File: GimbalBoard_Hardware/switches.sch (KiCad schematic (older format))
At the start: 31 parts

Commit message: connected everything up and changed power to accomodate teensy instead of tiva
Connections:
- net +3V3 renamed 3.3VL
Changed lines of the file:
@@
 $Descr A4 11693 8268
 encoding utf-8
-Sheet 4 7
+Sheet 4 8
 Title ""
 Date ""
@@
 $EndDescr
 $Comp
-L power:+3.3V #PWR?
-U 1 1 615E22D3
-P 1550 1200
-F 0 "#PWR?" H 1550 1050 50  0001 C CNN
-F 1 "+3.3V" H 1565 1373 50  0000 C CNN
-F 2 "" H 1550 1200 50  0001 C CNN
-F 3 "" H 1550 1200 50  0001 C CNN
-	1    1550 1200
-	1    0    0    -1
-$EndComp
-$Comp
 L Switch:SW_Push SW?
 U 1 1 615E41DD
@@
 Wire Wire Line
 	1550 5500 1550 4850
-$Comp
-L power:GND #PWR?
-U 1 1 615F842D
-P 3650 6300
-F 0 "#PWR?" H 3650 6050 50  0001 C CNN
-F 1 "GND" H 3655 6127 50  0000 C CNN
-F 2 "" H 3650 6300 50  0001 C CNN
-F 3 "" H 3650 6300 50  0001 C CNN
-	1    3650 6300
-	1    0    0    -1
-$EndComp
 Wire Wire Line
 	3350 1550 3650 1550
@@
 Wire Wire Line
 	3650 6150 3650 6300
-$Comp
-L power:+3.3V #PWR?
-U 1 1 61616E07
-P 4650 1450
-F 0 "#PWR?" H 4650 1300 50  0001 C CNN
-F 1 "+3.3V" H 4665 1623 50  0000 C CNN
-F 2 "" H 4650 1450 50  0001 C CNN
-F 3 "" H 4650 1450 50  0001 C CNN
-	1    4650 1450
-	1    0    0    -1
-$EndComp
 $Comp
 L Device:LED D?
@@
 Wire Wire Line
 	7400 2550 6650 2550
-$Comp
-L power:GND #PWR?
-U 1 1 61657CDC
-P 7400 3100
-F 0 "#PWR?" H 7400 2850 50  0001 C CNN
-F 1 "GND" H 7405 2927 50  0000 C CNN
-F 2 "" H 7400 3100 50  0001 C CNN
-F 3 "" H 7400 3100 50  0001 C CNN
-	1    7400 3100
-	1    0    0    -1
-$EndComp
 Wire Wire Line
 	5650 1900 5650 2150
@@
 Wire Wire Line
 	7400 1900 7400 2550
+Text HLabel 1550 1200 1    50   Input ~ 0
+3.3VL
+Text HLabel 3650 6300 3    50   Input ~ 0
+GND
+Text HLabel 4650 1450 1    50   Input ~ 0
+3.3VL
+Text HLabel 7400 3100 3    50   Input ~ 0
+GND
 $EndSCHEMATC

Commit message: added more text
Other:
- note added: "Digital/Manual Switch"
- note added: "Manual Servo Switches"
- moved on the sheet: D?, R?, SW?

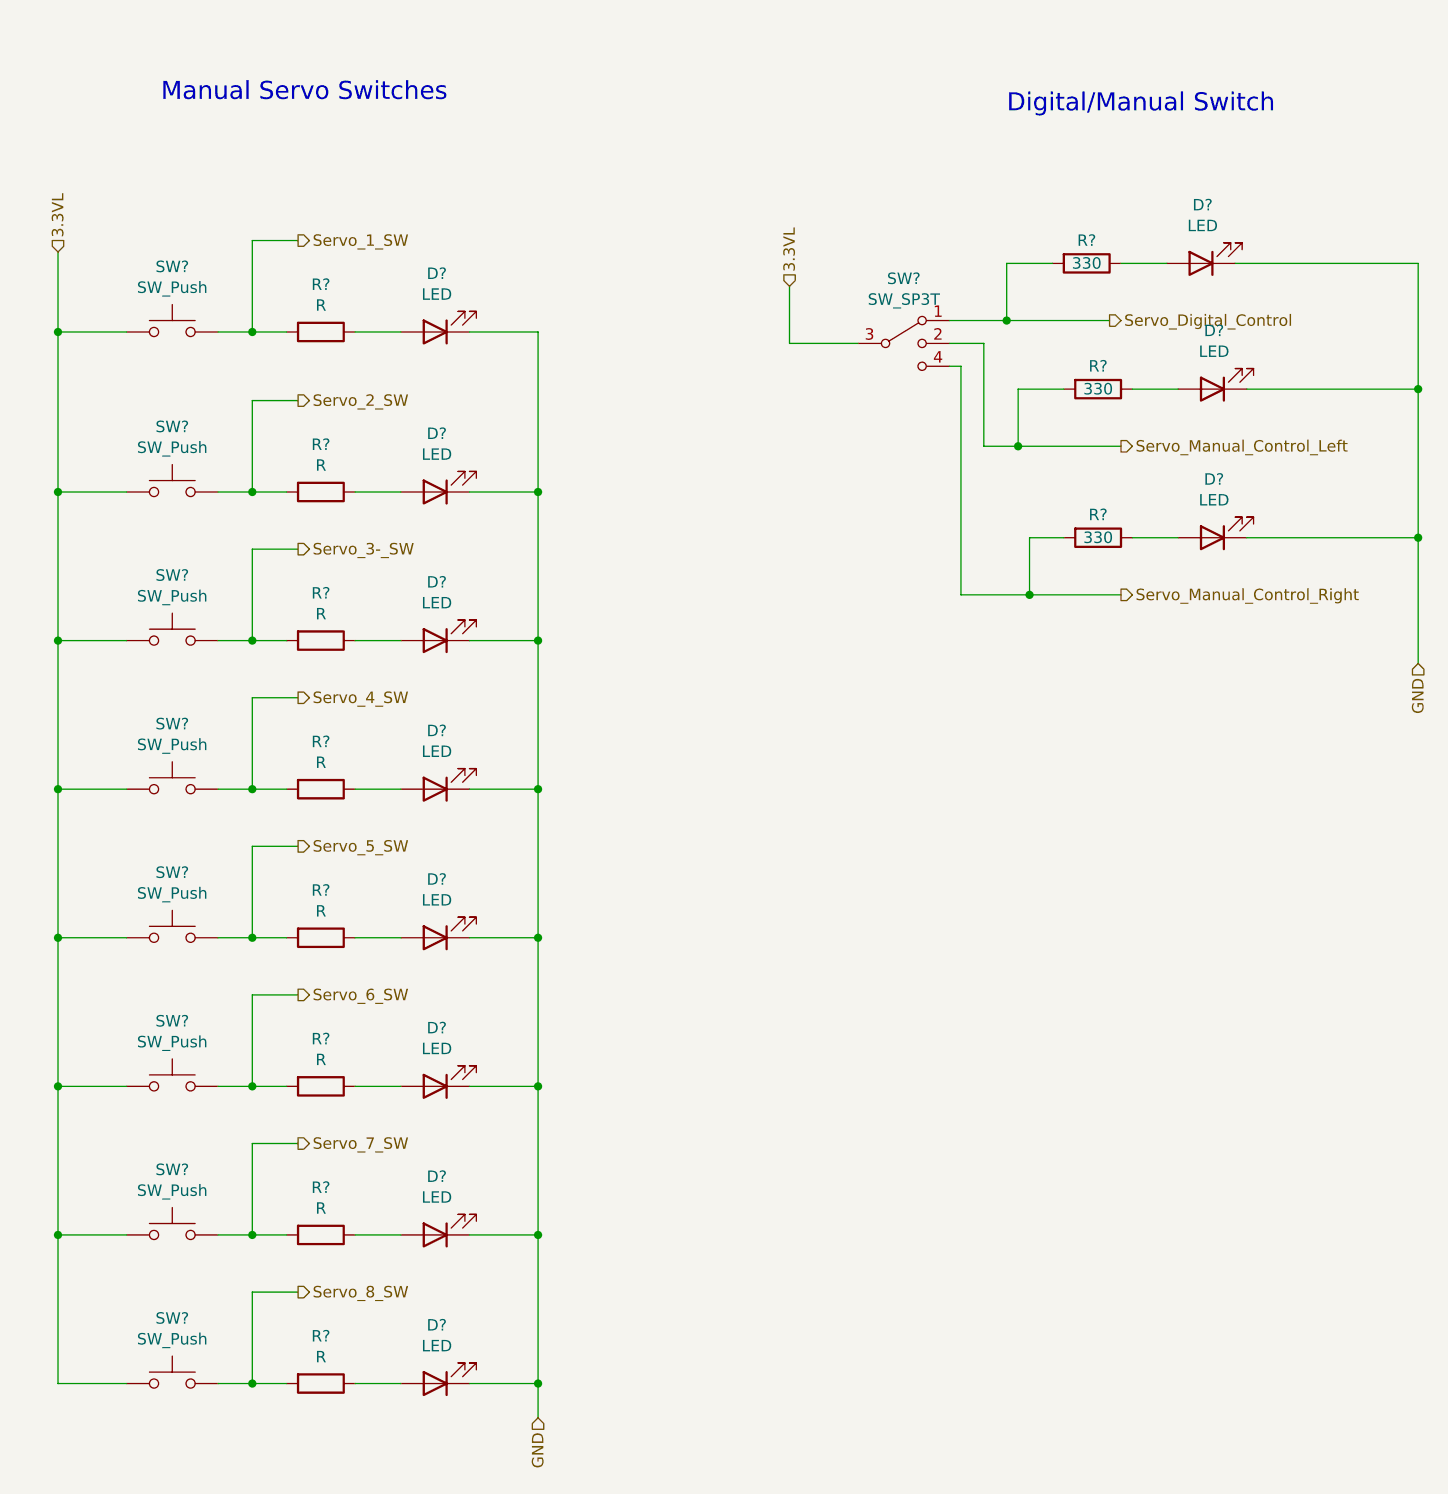
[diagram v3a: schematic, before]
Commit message: added labels, numbered everything, added no connection to pins. Still can't get past a couple pf errors in the electrical rules check
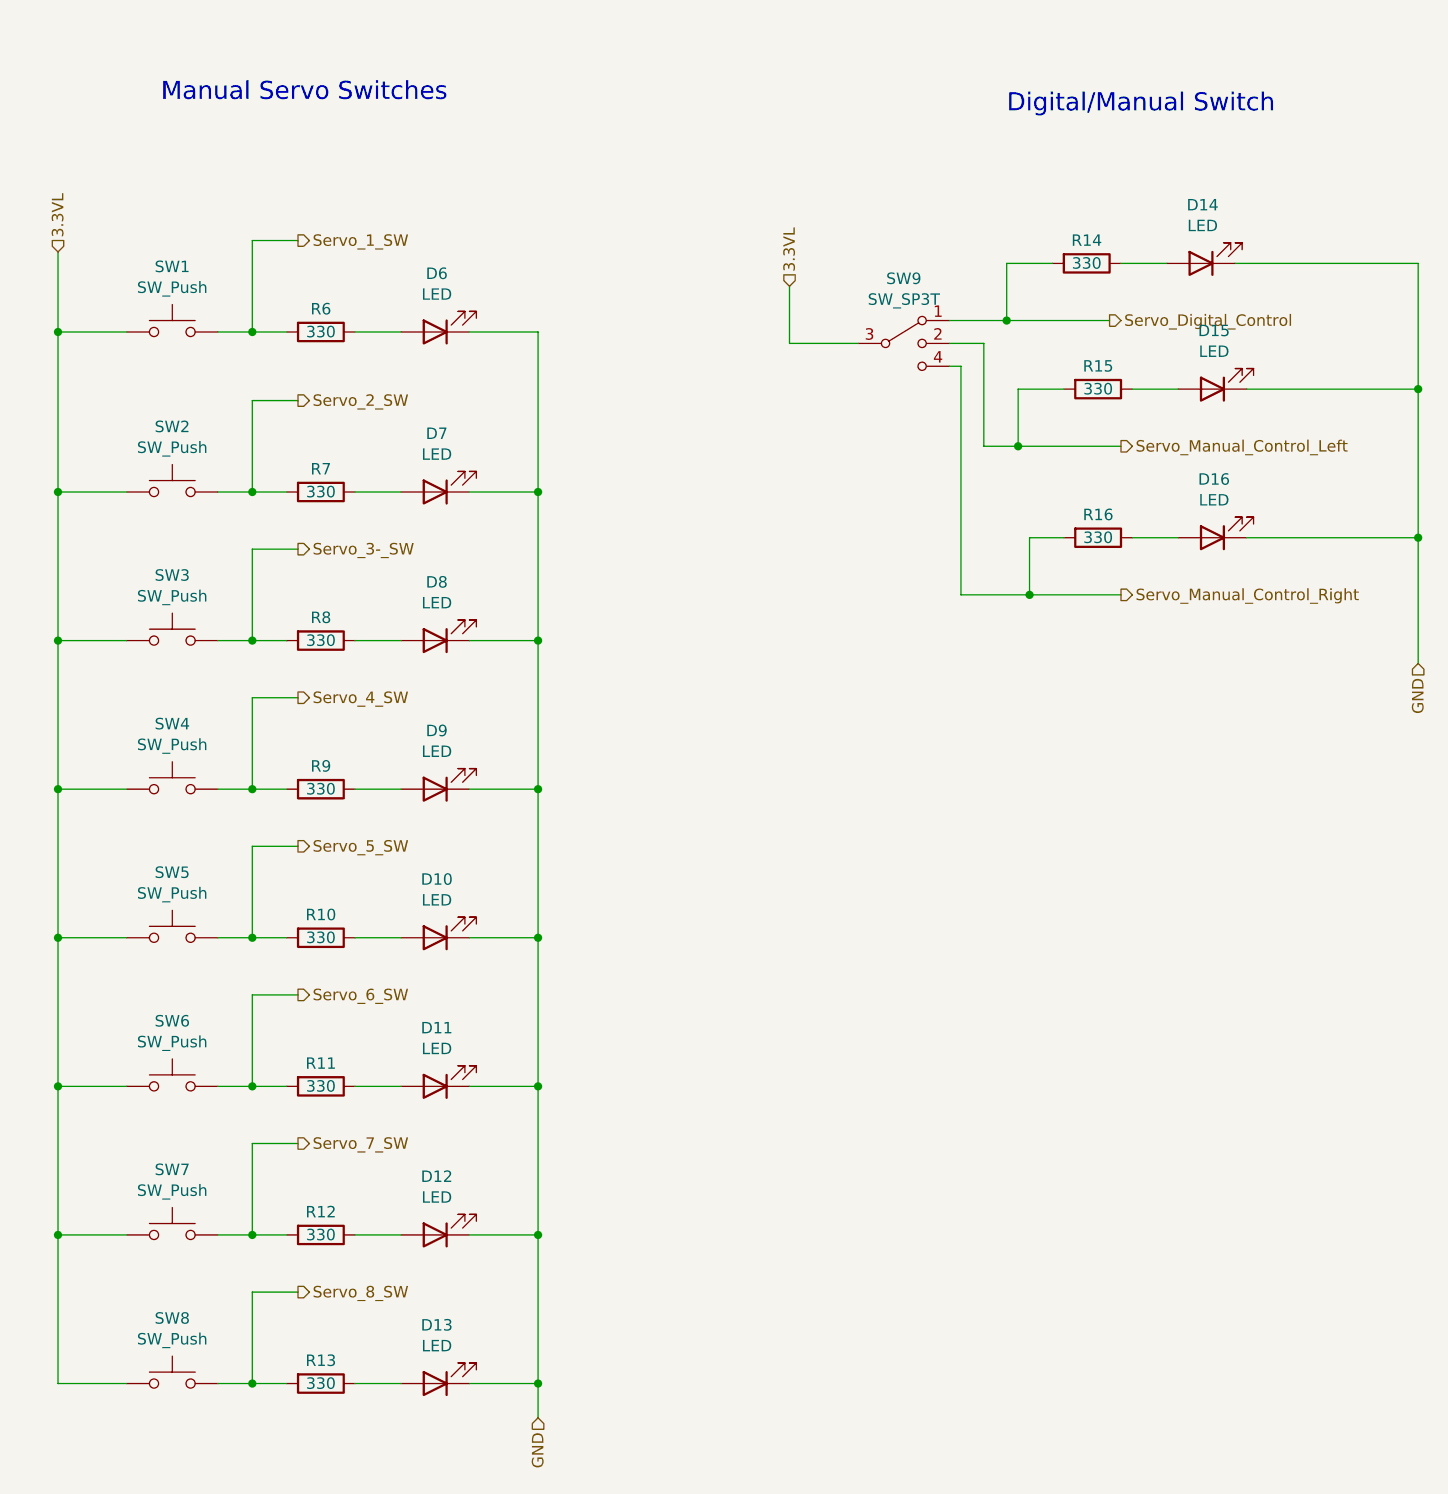
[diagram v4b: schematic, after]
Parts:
- R10, R11, R12, R13, R6, R7, R8, R9: renamed from R?; value R -> 330
- gave numbers to parts that had none: 23
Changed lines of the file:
@@
 $EndDescr
 $Comp
-L Switch:SW_Push SW?
+L Switch:SW_Push SW1
 U 1 1 615E41DD
 P 2100 2250
-F 0 "SW?" H 2100 2535 50  0000 C CNN
+F 0 "SW1" H 2100 2535 50  0000 C CNN
 F 1 "SW_Push" H 2100 2444 50  0000 C CNN
 F 2 "" H 2100 2450 50  0001 C CNN
@@
 $EndComp
 $Comp
-L Device:R R?
+L Device:R R6
 U 1 1 615E431C
 P 2750 2250
-F 0 "R?" V 2543 2250 50  0000 C CNN
-F 1 "R" V 2634 2250 50  0000 C CNN
+F 0 "R6" V 2650 2250 50  0000 C CNN
+F 1 "330" V 2750 2250 50  0000 C CNN
 F 2 "" V 2680 2250 50  0001 C CNN
 F 3 "~" H 2750 2250 50  0001 C CNN
@@
 $EndComp
 $Comp
-L Device:LED D?
+L Device:LED D6
 U 1 1 615E47F7
 P 3250 2250
-F 0 "D?" H 3243 1995 50  0000 C CNN
+F 0 "D6" H 3243 1995 50  0000 C CNN
 F 1 "LED" H 3243 2086 50  0000 C CNN
 F 2 "" H 3250 2250 50  0001 C CNN
@@
 	2900 2250 3100 2250
 $Comp
-L Switch:SW_Push SW?
+L Switch:SW_Push SW2
 U 1 1 615E8724
 P 2100 2950
-F 0 "SW?" H 2100 3235 50  0000 C CNN
+F 0 "SW2" H 2100 3235 50  0000 C CNN
 F 1 "SW_Push" H 2100 3144 50  0000 C CNN
 F 2 "" H 2100 3150 50  0001 C CNN
@@
 $EndComp
 $Comp
-L Device:R R?
+L Device:R R7
 U 1 1 615E872A
 P 2750 2950
-F 0 "R?" V 2543 2950 50  0000 C CNN
-F 1 "R" V 2634 2950 50  0000 C CNN
+F 0 "R7" V 2650 2950 50  0000 C CNN
+F 1 "330" V 2750 2950 50  0000 C CNN
 F 2 "" V 2680 2950 50  0001 C CNN
 F 3 "~" H 2750 2950 50  0001 C CNN
@@
 $EndComp
 $Comp
-L Device:LED D?
+L Device:LED D7
 U 1 1 615E8730
 P 3250 2950
-F 0 "D?" H 3243 2695 50  0000 C CNN
+F 0 "D7" H 3243 2695 50  0000 C CNN
 F 1 "LED" H 3243 2786 50  0000 C CNN
 F 2 "" H 3250 2950 50  0001 C CNN
@@
 	2900 2950 3100 2950
 $Comp
-L Switch:SW_Push SW?
+L Switch:SW_Push SW3
 U 1 1 615E9DC6
 P 2100 3600
-F 0 "SW?" H 2100 3885 50  0000 C CNN
+F 0 "SW3" H 2100 3885 50  0000 C CNN
 F 1 "SW_Push" H 2100 3794 50  0000 C CNN
 F 2 "" H 2100 3800 50  0001 C CNN
@@
 $EndComp
 $Comp
-L Device:R R?
+L Device:R R8
 U 1 1 615E9DCC
 P 2750 3600
-F 0 "R?" V 2543 3600 50  0000 C CNN
-F 1 "R" V 2634 3600 50  0000 C CNN
+F 0 "R8" V 2650 3600 50  0000 C CNN
+F 1 "330" V 2750 3600 50  0000 C CNN
 F 2 "" V 2680 3600 50  0001 C CNN
 F 3 "~" H 2750 3600 50  0001 C CNN
@@
 $EndComp
 $Comp
-L Device:LED D?
+L Device:LED D8
 U 1 1 615E9DD2
 P 3250 3600
-F 0 "D?" H 3243 3345 50  0000 C CNN
+F 0 "D8" H 3243 3345 50  0000 C CNN
 F 1 "LED" H 3243 3436 50  0000 C CNN
 F 2 "" H 3250 3600 50  0001 C CNN
@@
 	2900 3600 3100 3600
 $Comp
-L Switch:SW_Push SW?
+L Switch:SW_Push SW4
 U 1 1 615EAF7B
 P 2100 4250
-F 0 "SW?" H 2100 4535 50  0000 C CNN
+F 0 "SW4" H 2100 4535 50  0000 C CNN
 F 1 "SW_Push" H 2100 4444 50  0000 C CNN
 F 2 "" H 2100 4450 50  0001 C CNN
@@
 $EndComp
 $Comp
-L Device:R R?
+L Device:R R9
 U 1 1 615EAF81
 P 2750 4250
-F 0 "R?" V 2543 4250 50  0000 C CNN
-F 1 "R" V 2634 4250 50  0000 C CNN
+F 0 "R9" V 2650 4250 50  0000 C CNN
+F 1 "330" V 2750 4250 50  0000 C CNN
 F 2 "" V 2680 4250 50  0001 C CNN
 F 3 "~" H 2750 4250 50  0001 C CNN
@@
 $EndComp
 $Comp
-L Device:LED D?
+L Device:LED D9
 U 1 1 615EAF87
 P 3250 4250
-F 0 "D?" H 3243 3995 50  0000 C CNN
+F 0 "D9" H 3243 3995 50  0000 C CNN
 F 1 "LED" H 3243 4086 50  0000 C CNN
 F 2 "" H 3250 4250 50  0001 C CNN
@@
 	2900 4250 3100 4250
 $Comp
-L Switch:SW_Push SW?
+L Switch:SW_Push SW5
 U 1 1 615EBF82
 P 2100 4900
-F 0 "SW?" H 2100 5185 50  0000 C CNN
+F 0 "SW5" H 2100 5185 50  0000 C CNN
 F 1 "SW_Push" H 2100 5094 50  0000 C CNN
 F 2 "" H 2100 5100 50  0001 C CNN
@@
 $EndComp
 $Comp
-L Device:R R?
+L Device:R R10
 U 1 1 615EBF88
 P 2750 4900
-F 0 "R?" V 2543 4900 50  0000 C CNN
-F 1 "R" V 2634 4900 50  0000 C CNN
+F 0 "R10" V 2650 4900 50  0000 C CNN
+F 1 "330" V 2750 4900 50  0000 C CNN
 F 2 "" V 2680 4900 50  0001 C CNN
 F 3 "~" H 2750 4900 50  0001 C CNN
@@
 $EndComp
 $Comp
-L Device:LED D?
+L Device:LED D10
 U 1 1 615EBF8E
 P 3250 4900
-F 0 "D?" H 3243 4645 50  0000 C CNN
+F 0 "D10" H 3243 4645 50  0000 C CNN
 F 1 "LED" H 3243 4736 50  0000 C CNN
 F 2 "" H 3250 4900 50  0001 C CNN
@@
 	2900 4900 3100 4900
 $Comp
-L Switch:SW_Push SW?
+L Switch:SW_Push SW6
 U 1 1 615ECC88
 P 2100 5550
-F 0 "SW?" H 2100 5835 50  0000 C CNN
+F 0 "SW6" H 2100 5835 50  0000 C CNN
 F 1 "SW_Push" H 2100 5744 50  0000 C CNN
 F 2 "" H 2100 5750 50  0001 C CNN
@@
 $EndComp
 $Comp
-L Device:R R?
+L Device:R R11
 U 1 1 615ECC8E
 P 2750 5550
-F 0 "R?" V 2543 5550 50  0000 C CNN
-F 1 "R" V 2634 5550 50  0000 C CNN
+F 0 "R11" V 2650 5550 50  0000 C CNN
+F 1 "330" V 2750 5550 50  0000 C CNN
 F 2 "" V 2680 5550 50  0001 C CNN
 F 3 "~" H 2750 5550 50  0001 C CNN
@@
 $EndComp
 $Comp
-L Device:LED D?
+L Device:LED D11
 U 1 1 615ECC94
 P 3250 5550
-F 0 "D?" H 3243 5295 50  0000 C CNN
+F 0 "D11" H 3243 5295 50  0000 C CNN
 F 1 "LED" H 3243 5386 50  0000 C CNN
 F 2 "" H 3250 5550 50  0001 C CNN
@@
 	2900 5550 3100 5550
 $Comp
-L Switch:SW_Push SW?
+L Switch:SW_Push SW7
 U 1 1 615EE37A
 P 2100 6200
-F 0 "SW?" H 2100 6485 50  0000 C CNN
+F 0 "SW7" H 2100 6485 50  0000 C CNN
 F 1 "SW_Push" H 2100 6394 50  0000 C CNN
 F 2 "" H 2100 6400 50  0001 C CNN
@@
 $EndComp
 $Comp
-L Device:R R?
+L Device:R R12
 U 1 1 615EE380
 P 2750 6200
-F 0 "R?" V 2543 6200 50  0000 C CNN
-F 1 "R" V 2634 6200 50  0000 C CNN
+F 0 "R12" V 2650 6200 50  0000 C CNN
+F 1 "330" V 2750 6200 50  0000 C CNN
 F 2 "" V 2680 6200 50  0001 C CNN
 F 3 "~" H 2750 6200 50  0001 C CNN
@@
 $EndComp
 $Comp
-L Device:LED D?
+L Device:LED D12
 U 1 1 615EE386
 P 3250 6200
-F 0 "D?" H 3243 5945 50  0000 C CNN
+F 0 "D12" H 3243 5945 50  0000 C CNN
 F 1 "LED" H 3243 6036 50  0000 C CNN
 F 2 "" H 3250 6200 50  0001 C CNN
@@
 	2900 6200 3100 6200
 $Comp
-L Switch:SW_Push SW?
+L Switch:SW_Push SW8
 U 1 1 615EF3C5
 P 2100 6850
-F 0 "SW?" H 2100 7135 50  0000 C CNN
+F 0 "SW8" H 2100 7135 50  0000 C CNN
 F 1 "SW_Push" H 2100 7044 50  0000 C CNN
 F 2 "" H 2100 7050 50  0001 C CNN
@@
 $EndComp
 $Comp
-L Device:R R?
+L Device:R R13
 U 1 1 615EF3CB
 P 2750 6850
-F 0 "R?" V 2543 6850 50  0000 C CNN
-F 1 "R" V 2634 6850 50  0000 C CNN
+F 0 "R13" V 2650 6850 50  0000 C CNN
+F 1 "330" V 2750 6850 50  0000 C CNN
 F 2 "" V 2680 6850 50  0001 C CNN
 F 3 "~" H 2750 6850 50  0001 C CNN
@@
 $EndComp
 $Comp
-L Device:LED D?
+L Device:LED D13
 U 1 1 615EF3D1
 P 3250 6850
-F 0 "D?" H 3243 6595 50  0000 C CNN
+F 0 "D13" H 3243 6595 50  0000 C CNN
 F 1 "LED" H 3243 6686 50  0000 C CNN
 F 2 "" H 3250 6850 50  0001 C CNN
@@
 	3700 6850 3700 7000
 $Comp
-L Device:LED D?
+L Device:LED D14
 U 1 1 6161933E
 P 6600 1950
-F 0 "D?" H 6593 1695 50  0000 C CNN
+F 0 "D14" H 6593 1695 50  0000 C CNN
 F 1 "LED" H 6593 1786 50  0000 C CNN
 F 2 "" H 6600 1950 50  0001 C CNN
@@
 $EndComp
 $Comp
-L Device:R R?
+L Device:R R14
 U 1 1 6161A7C1
 P 6100 1950
-F 0 "R?" V 6000 1950 50  0000 C CNN
+F 0 "R14" V 6000 1950 50  0000 C CNN
 F 1 "330" V 6100 1950 50  0000 C CNN
 F 2 "" V 6030 1950 50  0001 C CNN
@@
 	5750 1950 5750 2200
 $Comp
-L Device:LED D?
+L Device:LED D15
 U 1 1 61657CB4
 P 6650 2500
-F 0 "D?" H 6643 2245 50  0000 C CNN
+F 0 "D15" H 6643 2245 50  0000 C CNN
 F 1 "LED" H 6643 2336 50  0000 C CNN
 F 2 "" H 6650 2500 50  0001 C CNN
@@
 $EndComp
 $Comp
-L Device:LED D?
+L Device:LED D16
 U 1 1 61657CBA
 P 6650 3150
-F 0 "D?" H 6643 2895 50  0000 C CNN
+F 0 "D16" H 6643 2895 50  0000 C CNN
 F 1 "LED" H 6643 2986 50  0000 C CNN
 F 2 "" H 6650 3150 50  0001 C CNN
@@
 $EndComp
 $Comp
-L Device:R R?
+L Device:R R15
 U 1 1 61657CC0
 P 6150 2500
-F 0 "R?" V 6050 2500 50  0000 C CNN
+F 0 "R15" V 6050 2500 50  0000 C CNN
 F 1 "330" V 6150 2500 50  0000 C CNN
 F 2 "" V 6080 2500 50  0001 C CNN
@@
 $EndComp
 $Comp
-L Device:R R?
+L Device:R R16
 U 1 1 61657CC6
 P 6150 3150
-F 0 "R?" V 6050 3150 50  0000 C CNN
+F 0 "R16" V 6050 3150 50  0000 C CNN
 F 1 "330" V 6150 3150 50  0000 C CNN
 F 2 "" V 6080 3150 50  0001 C CNN
@@
 	5800 2500 5800 2750
 $Comp
-L Switch:SW_SP3T SW?
+L Switch:SW_SP3T SW9
 U 1 1 6168F99A
 P 5300 2300
-F 0 "SW?" H 5300 2583 50  0000 C CNN
+F 0 "SW9" H 5300 2583 50  0000 C CNN
 F 1 "SW_SP3T" H 5300 2492 50  0000 C CNN
 F 2 "" H 4675 2475 50  0001 C CNN

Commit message: sheet has been reviewed
schematic has been reviewed. and resister values have been changed. as well as a ground being added
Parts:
- R10, R11, R12, R13, R14, R15, R16, R6, R7, R8, R9: value 330 -> 43
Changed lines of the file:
@@
 P 2750 2250
 F 0 "R6" V 2650 2250 50  0000 C CNN
-F 1 "330" V 2750 2250 50  0000 C CNN
+F 1 "43" V 2750 2250 50  0000 C CNN
 F 2 "" V 2680 2250 50  0001 C CNN
 F 3 "~" H 2750 2250 50  0001 C CNN
@@
 P 2750 2950
 F 0 "R7" V 2650 2950 50  0000 C CNN
-F 1 "330" V 2750 2950 50  0000 C CNN
+F 1 "43" V 2750 2950 50  0000 C CNN
 F 2 "" V 2680 2950 50  0001 C CNN
 F 3 "~" H 2750 2950 50  0001 C CNN
@@
 P 2750 3600
 F 0 "R8" V 2650 3600 50  0000 C CNN
-F 1 "330" V 2750 3600 50  0000 C CNN
+F 1 "43" V 2750 3600 50  0000 C CNN
 F 2 "" V 2680 3600 50  0001 C CNN
 F 3 "~" H 2750 3600 50  0001 C CNN
@@
 P 2750 4250
 F 0 "R9" V 2650 4250 50  0000 C CNN
-F 1 "330" V 2750 4250 50  0000 C CNN
+F 1 "43" V 2750 4250 50  0000 C CNN
 F 2 "" V 2680 4250 50  0001 C CNN
 F 3 "~" H 2750 4250 50  0001 C CNN
@@
 P 2750 4900
 F 0 "R10" V 2650 4900 50  0000 C CNN
-F 1 "330" V 2750 4900 50  0000 C CNN
+F 1 "43" V 2750 4900 50  0000 C CNN
 F 2 "" V 2680 4900 50  0001 C CNN
 F 3 "~" H 2750 4900 50  0001 C CNN
@@
 P 2750 5550
 F 0 "R11" V 2650 5550 50  0000 C CNN
-F 1 "330" V 2750 5550 50  0000 C CNN
+F 1 "43" V 2750 5550 50  0000 C CNN
 F 2 "" V 2680 5550 50  0001 C CNN
 F 3 "~" H 2750 5550 50  0001 C CNN
@@
 P 2750 6200
 F 0 "R12" V 2650 6200 50  0000 C CNN
-F 1 "330" V 2750 6200 50  0000 C CNN
+F 1 "43" V 2750 6200 50  0000 C CNN
 F 2 "" V 2680 6200 50  0001 C CNN
 F 3 "~" H 2750 6200 50  0001 C CNN
@@
 P 2750 6850
 F 0 "R13" V 2650 6850 50  0000 C CNN
-F 1 "330" V 2750 6850 50  0000 C CNN
+F 1 "43" V 2750 6850 50  0000 C CNN
 F 2 "" V 2680 6850 50  0001 C CNN
 F 3 "~" H 2750 6850 50  0001 C CNN
@@
 P 6100 1950
 F 0 "R14" V 6000 1950 50  0000 C CNN
-F 1 "330" V 6100 1950 50  0000 C CNN
+F 1 "43" V 6100 1950 50  0000 C CNN
 F 2 "" V 6030 1950 50  0001 C CNN
 F 3 "~" H 6100 1950 50  0001 C CNN
@@
 P 6150 2500
 F 0 "R15" V 6050 2500 50  0000 C CNN
-F 1 "330" V 6150 2500 50  0000 C CNN
+F 1 "43" V 6150 2500 50  0000 C CNN
 F 2 "" V 6080 2500 50  0001 C CNN
 F 3 "~" H 6150 2500 50  0001 C CNN
@@
 P 6150 3150
 F 0 "R16" V 6050 3150 50  0000 C CNN
-F 1 "330" V 6150 3150 50  0000 C CNN
+F 1 "43" V 6150 3150 50  0000 C CNN
 F 2 "" V 6080 3150 50  0001 C CNN
 F 3 "~" H 6150 3150 50  0001 C CNN
